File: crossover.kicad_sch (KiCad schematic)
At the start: 16 parts, among them J1 Power In, J2 Line In, J3 Tweeter Out, J4 Sub Out, U6 TL072

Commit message: Fix input section
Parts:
- removed C28, C29: 2.2u, Capacitor_THT:CP_Radial_D5.0mm_P2.50mm, symbol Device:C_Polarized_Small_US
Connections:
- net Left Input Buffer/In: now also J2.3 (Pin_3)
- net Right Input Buffer/In: now also J2.1 (Pin_1)
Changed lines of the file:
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@@
-    (stroke (width 0) (type default))
-  )
-  (wire (pts (xy 69.85 76.2) (xy 69.85 64.77))
     (stroke (width 0) (type default))
   )
@@
     (stroke (width 0) (type default))
   )
-  (wire (pts (xy 55.88 92.71) (xy 55.88 109.22))
+  (wire (pts (xy 55.88 87.63) (xy 55.88 109.22))
     (stroke (width 0) (type default))
   )
@@
   )
   (wire (pts (xy 220.98 113.03) (xy 220.98 109.22))
+    (stroke (width 0) (type default))
+  )
+  (wire (pts (xy 69.85 64.77) (xy 69.85 81.28))
     (stroke (width 0) (type default))
   )
@@
         )
       )
-    )
-  )
-  (symbol (lib_id "Device:C_Polarized_Small_US") (at 55.88 90.17 0) (unit 1)
-    (in_bom yes) (on_board yes) (dnp no) (fields_autoplaced)
-    (property "Reference" "C28" (at 58.42 88.4681 0)
-      (effects (font (size 1.27 1.27)) (justify left))
-    )
-    (property "Value" "2.2u" (at 58.42 91.0081 0)
-      (effects (font (size 1.27 1.27)) (justify left))
-    )
-    (property "Footprint" "Capacitor_THT:CP_Radial_D5.0mm_P2.50mm" (at 55.88 90.17 0)
-      (effects (font (size 1.27 1.27)) hide)
-    )
-    (property "Datasheet" "~" (at 55.88 90.17 0)
-      (effects (font (size 1.27 1.27)) hide)
-    )
-    (pin "1")
-    (pin "2")
-    (instances
-      (project "crossover"
-        (path "/3c8df2a5-e9f9-4495-af40-aa221f0b3fa5"
-          (reference "C28") (unit 1)
-        )
-      )
-    )
-  )
-  (symbol (lib_id "Device:C_Polarized_Small_US") (at 69.85 78.74 180) (unit 1)
-    (in_bom yes) (on_board yes) (dnp no) (fields_autoplaced)
-    (property "Reference" "C29" (at 72.39 77.9017 0)
-      (effects (font (size 1.27 1.27)) (justify right))
-    )
-    (property "Value" "2.2u" (at 72.39 80.4417 0)
-      (effects (font (size 1.27 1.27)) (justify right))
-    )
-    (property "Footprint" "Capacitor_THT:CP_Radial_D5.0mm_P2.50mm" (at 69.85 78.74 0)
-      (effects (font (size 1.27 1.27)) hide)
-    )
-    (property "Datasheet" "~" (at 69.85 78.74 0)
-      (effects (font (size 1.27 1.27)) hide)
-    )
-    (pin "1")
-    (pin "2")
-    (instances
-      (project "crossover"
-        (path "/3c8df2a5-e9f9-4495-af40-aa221f0b3fa5"
-          (reference "C29") (unit 1)
-        )
-      )

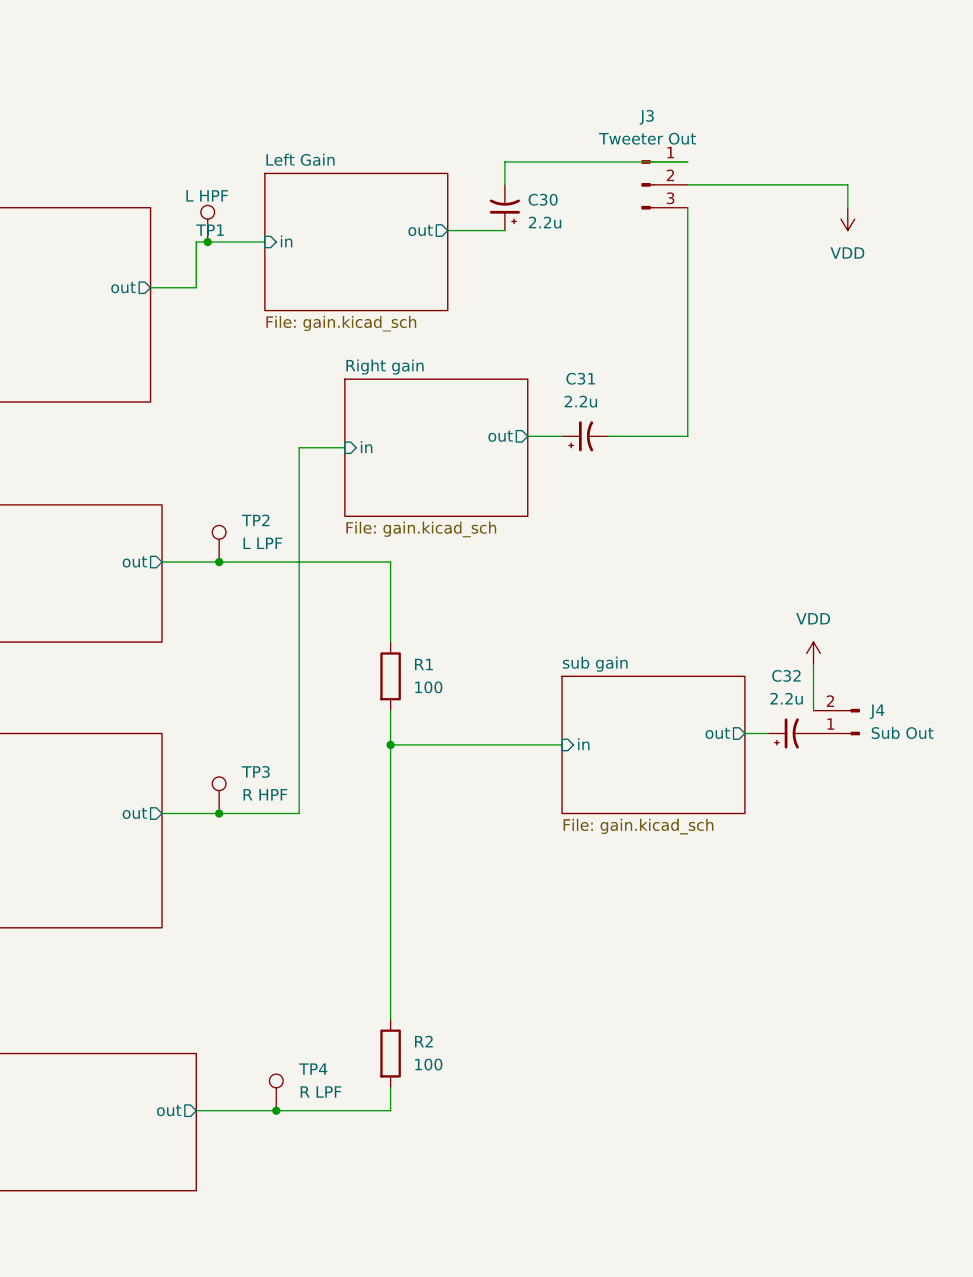
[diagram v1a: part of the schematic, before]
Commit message: Fix output filters
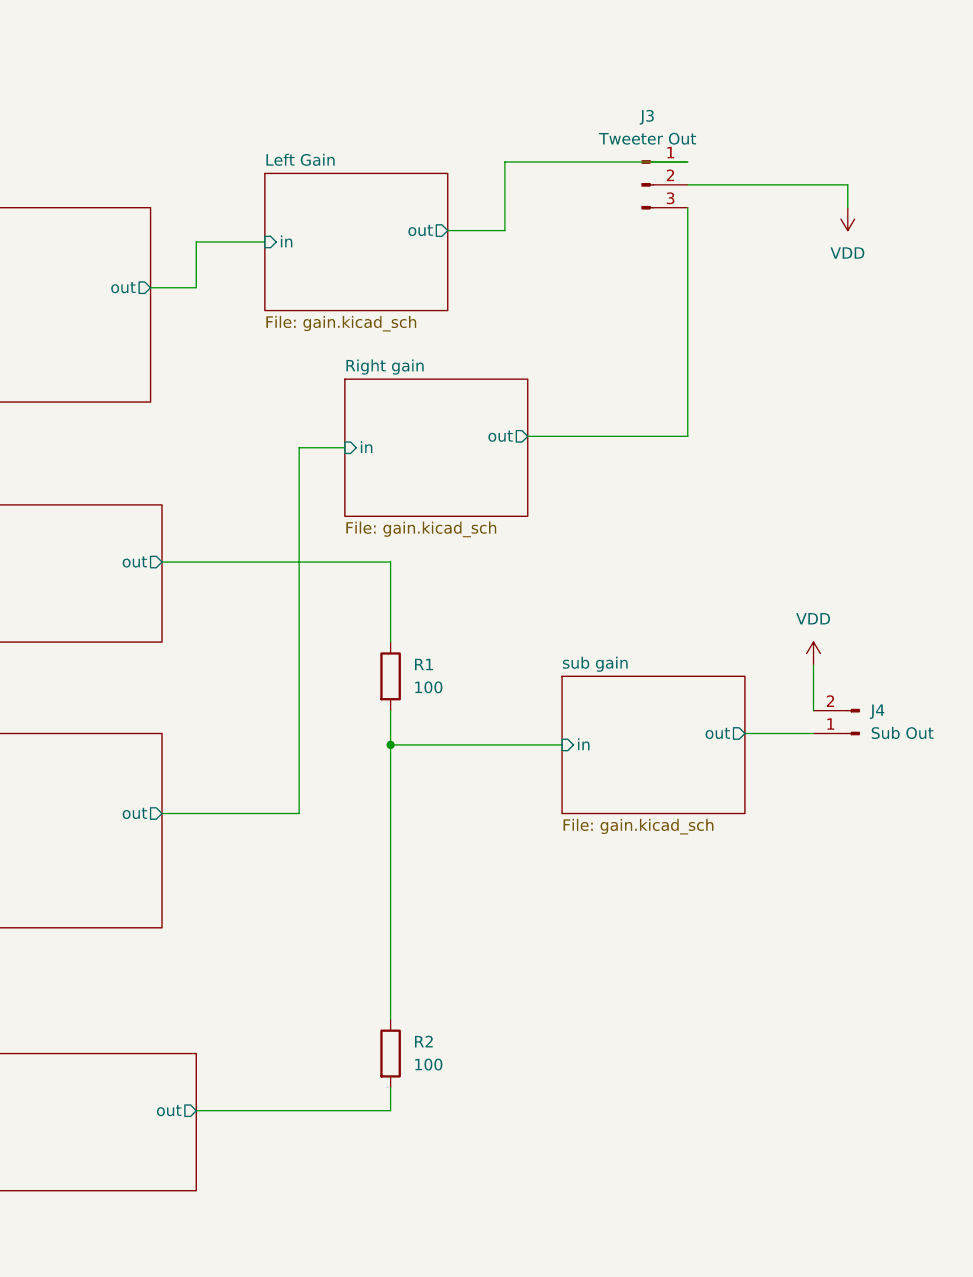
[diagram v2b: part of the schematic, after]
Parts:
- removed C30, C31, C32: 2.2u, Capacitor_THT:CP_Radial_D5.0mm_P2.50mm, symbol Device:C_Polarized_Small_US
- removed TP1: L HPF, TestPoint:TestPoint_Pad_1.0x1.0mm, symbol Connector:TestPoint
- removed TP2: L LPF, TestPoint:TestPoint_Pad_1.0x1.0mm, symbol Connector:TestPoint
- removed TP3: R HPF, TestPoint:TestPoint_Pad_1.0x1.0mm, symbol Connector:TestPoint
- removed TP4: R LPF, TestPoint:TestPoint_Pad_1.0x1.0mm, symbol Connector:TestPoint
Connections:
- net Left Gain/out: now also J3.1 (Pin_1)
- net Right gain/out: now also J3.3 (Pin_3)
- net sub gain/out: now also J4.1 (Pin_1)
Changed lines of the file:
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@@
 (kicad_sch (version 20230121) (generator eeschema)
   (paper "A4")
-  (junction (at 200.66 57.15) (diameter 0) (color 0 0 0 0)
-  )
-  (junction (at 208.28 153.67) (diameter 0) (color 0 0 0 0)
-  )
   (junction (at 146.05 121.92) (diameter 0) (color 0 0 0 0)
   )
-  (junction (at 201.93 120.65) (diameter 0) (color 0 0 0 0)
-  )
   (junction (at 137.16 63.5) (diameter 0) (color 0 0 0 0)
-  )
-  (junction (at 201.93 92.71) (diameter 0) (color 0 0 0 0)
   )
   (junction (at 220.98 113.03) (diameter 0) (color 0 0 0 0)
@@
   (no_connect (at 105.41 171.45))
   (no_connect (at 90.17 173.99))
-  (wire (pts (xy 201.93 92.71) (xy 220.98 92.71))
+  (wire (pts (xy 195.58 92.71) (xy 220.98 92.71))
     (stroke (width 0) (type default))
   )
@@
     (stroke (width 0) (type default))
   )
-  (wire (pts (xy 245.11 78.74) (xy 254 78.74))
+  (wire (pts (xy 236.22 78.74) (xy 254 78.74))
     (stroke (width 0) (type default))
   )
@@
     (stroke (width 0) (type default))
   )
-  (wire (pts (xy 236.22 78.74) (xy 240.03 78.74))
-    (stroke (width 0) (type default))
-  )
   (wire (pts (xy 240.03 113.03) (xy 220.98 113.03))
     (stroke (width 0) (type default))
@@
     (stroke (width 0) (type default))
   )
-  (wire (pts (xy 195.58 120.65) (xy 201.93 120.65))
+  (wire (pts (xy 195.58 120.65) (xy 210.82 120.65))
     (stroke (width 0) (type default))
   )
@@
     (stroke (width 0) (type default))
   )
-  (wire (pts (xy 195.58 92.71) (xy 201.93 92.71))
-    (stroke (width 0) (type default))
-  )
-  (wire (pts (xy 260.35 111.76) (xy 262.89 111.76))
+  (wire (pts (xy 260.35 111.76) (xy 267.97 111.76))
     (stroke (width 0) (type default))
   )
@@
     (stroke (width 0) (type default))
   )
-  (wire (pts (xy 233.68 50.8) (xy 233.68 48.26))
+  (wire (pts (xy 233.68 48.26) (xy 233.68 55.88))
     (stroke (width 0) (type default))
   )
@@
     (stroke (width 0) (type default))
   )
-  (wire (pts (xy 199.39 57.15) (xy 200.66 57.15))
-    (stroke (width 0) (type default))
-  )
   (wire (pts (xy 220.98 113.03) (xy 220.98 109.22))
     (stroke (width 0) (type default))
@@
     (stroke (width 0) (type default))
   )
-  (wire (pts (xy 200.66 57.15) (xy 207.01 57.15))
+  (wire (pts (xy 199.39 57.15) (xy 207.01 57.15))
     (stroke (width 0) (type default))
   )
@@
     (stroke (width 0) (type default))
   )
-  (wire (pts (xy 208.28 153.67) (xy 220.98 153.67))
-    (stroke (width 0) (type default))
-  )
   (wire (pts (xy 154.94 93.98) (xy 137.16 93.98))
     (stroke (width 0) (type default))
@@
     (stroke (width 0) (type default))
   )
-  (wire (pts (xy 199.39 153.67) (xy 208.28 153.67))
-    (stroke (width 0) (type default))
-  )
-  (wire (pts (xy 201.93 120.65) (xy 210.82 120.65))
+  (wire (pts (xy 199.39 153.67) (xy 220.98 153.67))
     (stroke (width 0) (type default))
   )
@@
         (path "/3c8df2a5-e9f9-4495-af40-aa221f0b3fa5"
           (reference "J2") (unit 1)
-        )
-      )
-    )
-  )
-  (symbol (lib_id "Connector:TestPoint") (at 201.93 92.71 0) (unit 1)
-    (in_bom yes) (on_board yes) (dnp no) (fields_autoplaced)
-    (property "Reference" "TP2" (at 204.47 88.1379 0)
-      (effects (font (size 1.27 1.27)) (justify left))
-    )
-    (property "Value" "L LPF" (at 204.47 90.6779 0)
-      (effects (font (size 1.27 1.27)) (justify left))
-    )
-    (property "Footprint" "TestPoint:TestPoint_Pad_1.0x1.0mm" (at 207.01 92.71 0)
-      (effects (font (size 1.27 1.27)) hide)
-    )
-    (property "Datasheet" "~" (at 207.01 92.71 0)
-      (effects (font (size 1.27 1.27)) hide)
-    )
-    (pin "1")
-    (instances
-      (project "crossover"
-        (path "/3c8df2a5-e9f9-4495-af40-aa221f0b3fa5"
-          (reference "TP2") (unit 1)
         )
       )
@@
     )
   )
-  (symbol (lib_id "Device:C_Polarized_Small_US") (at 233.68 53.34 180) (unit 1)
-    (in_bom yes) (on_board yes) (dnp no) (fields_autoplaced)
-    (property "Reference" "C30" (at 236.22 52.5017 0)
-      (effects (font (size 1.27 1.27)) (justify right))
-    )
-    (property "Value" "2.2u" (at 236.22 55.0417 0)
-      (effects (font (size 1.27 1.27)) (justify right))
-    )
-    (property "Footprint" "Capacitor_THT:CP_Radial_D5.0mm_P2.50mm" (at 233.68 53.34 0)
-      (effects (font (size 1.27 1.27)) hide)
-    )
-    (property "Datasheet" "~" (at 233.68 53.34 0)
-      (effects (font (size 1.27 1.27)) hide)
-    )
-    (pin "1")
-    (pin "2")
-    (instances
-      (project "crossover"
-        (path "/3c8df2a5-e9f9-4495-af40-aa221f0b3fa5"
-          (reference "C30") (unit 1)
-        )
-      )
-    )
-  )
   (symbol (lib_id "power:VDD") (at 267.97 104.14 0) (unit 1)
     (in_bom yes) (on_board yes) (dnp no) (fields_autoplaced)
@@
         (path "/3c8df2a5-e9f9-4495-af40-aa221f0b3fa5"
           (reference "#PWR02") (unit 1)
-        )
-      )
-    )
-  )
-  (symbol (lib_id "Device:C_Polarized_Small_US") (at 265.43 111.76 90) (unit 1)
-    (in_bom yes) (on_board yes) (dnp no) (fields_autoplaced)
-    (property "Reference" "C32" (at 264.9982 105.41 90)
-      (effects (font (size 1.27 1.27)))
-    )
-    (property "Value" "2.2u" (at 264.9982 107.95 90)
-      (effects (font (size 1.27 1.27)))
-    )
-    (property "Footprint" "Capacitor_THT:CP_Radial_D5.0mm_P2.50mm" (at 265.43 111.76 0)
-      (effects (font (size 1.27 1.27)) hide)
-    )
-    (property "Datasheet" "~" (at 265.43 111.76 0)
-      (effects (font (size 1.27 1.27)) hide)
-    )
-    (pin "1")
-    (pin "2")
-    (instances
-      (project "crossover"
-        (path "/3c8df2a5-e9f9-4495-af40-aa221f0b3fa5"
-          (reference "C32") (unit 1)
         )
       )
@@
     )
   )
-  (symbol (lib_id "Connector:TestPoint") (at 201.93 120.65 0) (unit 1)
-    (in_bom yes) (on_board yes) (dnp no) (fields_autoplaced)
-    (property "Reference" "TP3" (at 204.47 116.0779 0)
-      (effects (font (size 1.27 1.27)) (justify left))
-    )
-    (property "Value" "R HPF" (at 204.47 118.6179 0)
-      (effects (font (size 1.27 1.27)) (justify left))
-    )
-    (property "Footprint" "TestPoint:TestPoint_Pad_1.0x1.0mm" (at 207.01 120.65 0)
-      (effects (font (size 1.27 1.27)) hide)
-    )
-    (property "Datasheet" "~" (at 207.01 120.65 0)
-      (effects (font (size 1.27 1.27)) hide)
-    )
-    (pin "1")
-    (instances
-      (project "crossover"
-        (path "/3c8df2a5-e9f9-4495-af40-aa221f0b3fa5"
-          (reference "TP3") (unit 1)
-        )
-      )
-    )
-  )
   (symbol (lib_id "Connector:Conn_01x02_Male") (at 20.32 33.02 0) (unit 1)
     (in_bom yes) (on_board yes) (dnp no) (fields_autoplaced)
@@
     )
   )
-  (symbol (lib_id "Connector:TestPoint") (at 200.66 57.15 0) (unit 1)
-    (in_bom yes) (on_board yes) (dnp no)
-    (property "Reference" "TP1" (at 199.39 55.88 0)
-      (effects (font (size 1.27 1.27)) (justify left))
-    )
-    (property "Value" "L HPF" (at 198.12 52.07 0)
-      (effects (font (size 1.27 1.27)) (justify left))
-    )
-    (property "Footprint" "TestPoint:TestPoint_Pad_1.0x1.0mm" (at 205.74 57.15 0)
-      (effects (font (size 1.27 1.27)) hide)
-    )
-    (property "Datasheet" "~" (at 205.74 57.15 0)
-      (effects (font (size 1.27 1.27)) hide)
-    )
-    (pin "1")
-    (instances
-      (project "crossover"
-        (path "/3c8df2a5-e9f9-4495-af40-aa221f0b3fa5"
-          (reference "TP1") (unit 1)
-        )
-      )
-    )
-  )
   (symbol (lib_id "power:VDD") (at 271.78 53.34 180) (unit 1)
     (in_bom yes) (on_board yes) (dnp no) (fields_autoplaced)
@@
         (path "/3c8df2a5-e9f9-4495-af40-aa221f0b3fa5"
           (reference "#PWR03") (unit 1)
-        )
-      )
-    )
-  )
-  (symbol (lib_id "Device:C_Polarized_Small_US") (at 242.57 78.74 90) (unit 1)
-    (in_bom yes) (on_board yes) (dnp no) (fields_autoplaced)
-    (property "Reference" "C31" (at 242.1382 72.39 90)
-      (effects (font (size 1.27 1.27)))
-    )
-    (property "Value" "2.2u" (at 242.1382 74.93 90)
-      (effects (font (size 1.27 1.27)))
-    )
-    (property "Footprint" "Capacitor_THT:CP_Radial_D5.0mm_P2.50mm" (at 242.57 78.74 0)
-      (effects (font (size 1.27 1.27)) hide)
-    )
-    (property "Datasheet" "~" (at 242.57 78.74 0)
-      (effects (font (size 1.27 1.27)) hide)
-    )
-    (pin "1")
-    (pin "2")
-    (instances
-      (project "crossover"
-        (path "/3c8df2a5-e9f9-4495-af40-aa221f0b3fa5"
-          (reference "C31") (unit 1)
         )
       )
@@
         )
       )
-    )
-  )
-  (symbol (lib_id "Connector:TestPoint") (at 208.28 153.67 0) (unit 1)
-    (in_bom yes) (on_board yes) (dnp no) (fields_autoplaced)
-    (property "Reference" "TP4" (at 210.82 149.0979 0)
-      (effects (font (size 1.27 1.27)) (justify left))
-    )
-    (property "Value" "R LPF" (at 210.82 151.6379 0)
-      (effects (font (size 1.27 1.27)) (justify left))
-    )
-    (property "Footprint" "TestPoint:TestPoint_Pad_1.0x1.0mm" (at 213.36 153.67 0)
-      (effects (font (size 1.27 1.27)) hide)
-    )
-    (property "Datasheet" "~" (at 213.36 153.67 0)
-      (effects (font (size 1.27 1.27)) hide)
-    )
-    (pin "1")
-    (instances
-      (project "crossover"
-        (path "/3c8df2a5-e9f9-4495-af40-aa221f0b3fa5"
-          (reference "TP4") (unit 1)
-        )
-      )
